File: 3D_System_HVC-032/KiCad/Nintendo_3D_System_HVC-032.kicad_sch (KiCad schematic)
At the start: 45 parts, among them CN1 Famicon Expansion Port, J1 スコープ１, J2 スコープ２, Q1 2SC2120, U1 Sharp IX0043AE, U2 JRC 4558D, X1 4MHz

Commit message: Update Nintendo_3D_System_HVC-032.kicad_sch
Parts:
- C1, C10, C11, C12, C6, C7, C8, C9: footprint (none) -> Capacitor_THT:CP_Radial_D5.0mm_P2.50mm
- C2, C4, C5: footprint (none) -> Capacitor_THT:C_Disc_D3.4mm_W2.1mm_P2.50mm
- CN1: footprint (none) -> Connector_PinHeader_2.54mm:PinHeader_1x03_P2.54mm_Vertical
- D2, D3, D4, D5, D6, ZD1: footprint (none) -> Diode_THT:D_DO-35_SOD27_P7.62mm_Horizontal
- FB1: footprint (none) -> Clueless_Engineer:FB_28L0138-10R-10
- J1, J2: footprint (none) -> Connector_Audio:Jack_3.5mm_CUI_SJ1-3513N_Horizontal
- L1: footprint (none) -> Inductor_THT:L_Axial_L16.0mm_D7.5mm_P25.40mm_Horizontal_Fastron_XHBCC
- Q1: footprint (none) -> Package_TO_SOT_THT:TO-92_Inline
- R1, R10, R11, R12, R13, R14, R15, R16, R17, R18, R19, R2, R3, R4, R5, R6, R7, R8, R9: footprint (none) -> Resistor_THT:R_Axial_DIN0207_L6.3mm_D2.5mm_P7.62mm_Horizontal
- U2: footprint (none) -> Package_DIP:DIP-8_W7.62mm
- X1: footprint (none) -> Crystal:Crystal_HC49-U_Vertical
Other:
- moved on the sheet: C10
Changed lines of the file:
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@@
 		)
 	)
-	(text_box "ZD1 original likely a RD15EB"
+	(text_box "ZD1 original likely an RD15EB"
 		(exclude_from_sim no)
 		(at 143.51 46.99 0)
-		(size 17.78 6.35)
+		(size 19.05 5.08)
 		(margins 0.9525 0.9525 0.9525 0.9525)
 		(stroke
@@
 	(wire
 		(pts
-			(xy 223.52 59.69) (xy 223.52 54.61)
-		)
-		(stroke
-			(width 0)
-			(type default)
-		)
-	)
-	(wire
-		(pts
 			(xy 152.4 63.5) (xy 149.86 63.5)
 		)
@@
 	(wire
 		(pts
-			(xy 223.52 49.53) (xy 223.52 52.07)
+			(xy 223.52 49.53) (xy 223.52 50.8)
 		)
 		(stroke
@@
 	(wire
 		(pts
+			(xy 223.52 58.42) (xy 223.52 59.69)
+		)
+		(stroke
+			(width 0)
+			(type default)
+		)
+	)
+	(wire
+		(pts
 			(xy 80.01 66.04) (xy 87.63 66.04)
 		)
@@
 			)
 		)
-		(property "Footprint" ""
+		(property "Footprint" "Resistor_THT:R_Axial_DIN0207_L6.3mm_D2.5mm_P7.62mm_Horizontal"
 			(at 184.912 74.93 90)
 			(effects
@@
 			)
 		)
-		(property "Footprint" ""
+		(property "Footprint" "Package_DIP:DIP-8_W7.62mm"
 			(at 245.11 46.99 0)
 			(effects
@@
 			)
 		)
-		(property "Footprint" ""
+		(property "Footprint" "Resistor_THT:R_Axial_DIN0207_L6.3mm_D2.5mm_P7.62mm_Horizontal"
 			(at 156.21 65.278 90)
 			(effects
@@
 			)
 		)
-		(property "Footprint" ""
+		(property "Footprint" "Diode_THT:D_DO-35_SOD27_P7.62mm_Horizontal"
 			(at 163.83 43.18 0)
 			(effects
@@
 			)
 		)
-		(property "Footprint" ""
+		(property "Footprint" "Resistor_THT:R_Axial_DIN0207_L6.3mm_D2.5mm_P7.62mm_Horizontal"
 			(at 101.092 175.26 90)
 			(effects
@@
 			)
 		)
-		(property "Footprint" ""
+		(property "Footprint" "Capacitor_THT:CP_Radial_D5.0mm_P2.50mm"
 			(at 21.2852 72.39 0)
 			(effects
@@
 			)
 		)
-		(property "Footprint" ""
+		(property "Footprint" "Resistor_THT:R_Axial_DIN0207_L6.3mm_D2.5mm_P7.62mm_Horizontal"
 			(at 57.15 128.778 90)
 			(effects
@@
 			)
 		)
-		(property "Footprint" ""
+		(property "Footprint" "Resistor_THT:R_Axial_DIN0207_L6.3mm_D2.5mm_P7.62mm_Horizontal"
 			(at 77.47 142.748 90)
 			(effects
@@
 			)
 		)
-		(property "Footprint" ""
+		(property "Footprint" "Clueless_Engineer:FB_28L0138-10R-10"
 			(at 98.552 49.53 90)
 			(effects
@@
 			)
 		)
-		(property "Footprint" ""
+		(property "Footprint" "Inductor_THT:L_Axial_L16.0mm_D7.5mm_P25.40mm_Horizontal_Fastron_XHBCC"
 			(at 186.69 31.75 0)
 			(effects
@@
 			)
 		)
-		(property "Footprint" ""
+		(property "Footprint" "Package_DIP:DIP-8_W7.62mm"
 			(at 76.2 168.91 0)
 			(effects
@@
 			)
 		)
-		(property "Footprint" ""
+		(property "Footprint" "Resistor_THT:R_Axial_DIN0207_L6.3mm_D2.5mm_P7.62mm_Horizontal"
 			(at 57.15 62.738 90)
 			(effects
@@
 			)
 		)
-		(property "Footprint" ""
+		(property "Footprint" "Connector_PinHeader_2.54mm:PinHeader_1x03_P2.54mm_Vertical"
 			(at 33.02 60.96 0)
 			(effects
@@
 			)
 		)
-		(property "Footprint" ""
+		(property "Footprint" "Capacitor_THT:CP_Radial_D5.0mm_P2.50mm"
 			(at 100.33 128.5748 0)
 			(effects
@@
 			)
 		)
-		(property "Footprint" ""
+		(property "Footprint" "Diode_THT:D_DO-35_SOD27_P7.62mm_Horizontal"
 			(at 149.86 74.93 0)
 			(effects
@@
 			)
 		)
-		(property "Footprint" ""
+		(property "Footprint" "Resistor_THT:R_Axial_DIN0207_L6.3mm_D2.5mm_P7.62mm_Horizontal"
 			(at 55.88 169.672 90)
 			(effects
@@
 			)
 		)
-		(property "Footprint" ""
+		(property "Footprint" "Diode_THT:D_DO-35_SOD27_P7.62mm_Horizontal"
 			(at 205.74 41.91 0)
 			(effects
@@
 	(symbol
 		(lib_id "Device:C_Polarized")
-		(at 223.52 55.88 0)
+		(at 223.52 54.61 0)
 		(unit 1)
 		(exclude_from_sim no)
@@
 		(fields_autoplaced yes)
 		(property "Reference" "C10"
-			(at 227.33 53.7209 0)
+			(at 227.33 52.4509 0)
 			(effects
 				(font
@@
 		)
 		(property "Value" "22µF 16V"
-			(at 227.33 56.2609 0)
+			(at 227.33 54.9909 0)
 			(effects
 				(font
@@
 			)
 		)
-		(property "Footprint" ""
-			(at 224.4852 59.69 0)
+		(property "Footprint" "Capacitor_THT:CP_Radial_D5.0mm_P2.50mm"
+			(at 224.4852 58.42 0)
 			(effects
 				(font
@@
 		)
 		(property "Datasheet" "~"
-			(at 223.52 55.88 0)
+			(at 223.52 54.61 0)
 			(effects
 				(font
@@
 		)
 		(property "Description" "Polarized capacitor"
-			(at 223.52 55.88 0)
+			(at 223.52 54.61 0)
 			(effects
 				(font
@@
 			)
 		)
-		(property "Footprint" ""
+		(property "Footprint" "Resistor_THT:R_Axial_DIN0207_L6.3mm_D2.5mm_P7.62mm_Horizontal"
 			(at 60.452 160.02 90)
 			(effects
@@
 			)
 		)
-		(property "Footprint" ""
+		(property "Footprint" "Resistor_THT:R_Axial_DIN0207_L6.3mm_D2.5mm_P7.62mm_Horizontal"
 			(at 132.842 55.88 90)
 			(effects
@@
 			)
 		)
-		(property "Footprint" ""
+		(property "Footprint" "Capacitor_THT:CP_Radial_D5.0mm_P2.50mm"
 			(at 203.2 35.8648 0)
 			(effects
@@
 			)
 		)
-		(property "Footprint" ""
+		(property "Footprint" "Resistor_THT:R_Axial_DIN0207_L6.3mm_D2.5mm_P7.62mm_Horizontal"
 			(at 55.88 168.148 90)
 			(effects
@@
 			)
 		)
-		(property "Footprint" ""
+		(property "Footprint" "Resistor_THT:R_Axial_DIN0207_L6.3mm_D2.5mm_P7.62mm_Horizontal"
 			(at 105.918 134.62 90)
 			(effects
@@
 			)
 		)
-		(property "Footprint" ""
+		(property "Footprint" "Resistor_THT:R_Axial_DIN0207_L6.3mm_D2.5mm_P7.62mm_Horizontal"
 			(at 65.278 119.38 90)
 			(effects
@@
 			)
 		)
-		(property "Footprint" ""
+		(property "Footprint" "Resistor_THT:R_Axial_DIN0207_L6.3mm_D2.5mm_P7.62mm_Horizontal"
 			(at 111.76 170.688 90)
 			(effects
@@
 			)
 		)
-		(property "Footprint" ""
+		(property "Footprint" "Package_TO_SOT_THT:TO-92_Inline"
 			(at 247.65 63.5 0)
 			(effects
@@
 			)
 		)
-		(property "Footprint" ""
+		(property "Footprint" "Resistor_THT:R_Axial_DIN0207_L6.3mm_D2.5mm_P7.62mm_Horizontal"
 			(at 165.608 74.93 90)
 			(effects
@@
 			)
 		)
-		(property "Footprint" ""
+		(property "Footprint" "Resistor_THT:R_Axial_DIN0207_L6.3mm_D2.5mm_P7.62mm_Horizontal"
 			(at 68.072 55.88 90)
 			(effects
@@
 			)
 		)
-		(property "Footprint" ""
+		(property "Footprint" "Capacitor_THT:C_Disc_D3.4mm_W2.1mm_P2.50mm"
 			(at 95.25 44.7548 0)
 			(effects
@@
 			)
 		)
-		(property "Footprint" ""
+		(property "Footprint" "Resistor_THT:R_Axial_DIN0207_L6.3mm_D2.5mm_P7.62mm_Horizontal"
 			(at 76.2 182.118 90)
 			(effects
@@
 			)
 		)
-		(property "Footprint" ""
+		(property "Footprint" "Diode_THT:D_DO-35_SOD27_P7.62mm_Horizontal"
 			(at 158.75 36.83 0)
 			(effects
@@
 			)
 		)
-		(property "Footprint" ""
+		(property "Footprint" "Capacitor_THT:CP_Radial_D5.0mm_P2.50mm"
 			(at 147.32 62.5348 0)
 			(effects
@@
 			)
 		)
-		(property "Footprint" ""
+		(property "Footprint" "Connector_Audio:Jack_3.5mm_CUI_SJ1-3513N_Horizontal"
 			(at 133.35 129.54 0)
 			(effects
@@
 			)
 		)
-		(property "Footprint" ""
+		(property "Footprint" "Connector_Audio:Jack_3.5mm_CUI_SJ1-3513N_Horizontal"
 			(at 132.08 171.45 0)
 			(effects
@@
 			)
 		)
-		(property "Footprint" ""
+		(property "Footprint" "Capacitor_THT:C_Disc_D3.4mm_W2.1mm_P2.50mm"
 			(at 58.42 75.2348 0)
 			(effects
@@
 			)
 		)
-		(property "Footprint" ""
+		(property "Footprint" "Capacitor_THT:CP_Radial_D5.0mm_P2.50mm"
 			(at 99.06 167.9448 0)
 			(effects
@@
 			)
 		)
-		(property "Footprint" ""
+		(property "Footprint" "Crystal:Crystal_HC49-U_Vertical"
 			(at 74.93 80.01 0)
 			(effects
@@
 			)
 		)
-		(property "Footprint" ""
+		(property "Footprint" "Diode_THT:D_DO-35_SOD27_P7.62mm_Horizontal"
 			(at 212.09 36.83 0)
 			(effects
@@
 			)
 		)
-		(property "Footprint" ""
+		(property "Footprint" "Resistor_THT:R_Axial_DIN0207_L6.3mm_D2.5mm_P7.62mm_Horizontal"
 			(at 57.15 133.858 90)
 			(effects
@@
 			)
 		)
-		(property "Footprint" ""
+		(property "Footprint" "Capacitor_THT:CP_Radial_D5.0mm_P2.50mm"
 			(at 168.91 37.7952 0)
 			(effects
@@
 			)
 		)
-		(property "Footprint" ""
+		(property "Footprint" "Resistor_THT:R_Axial_DIN0207_L6.3mm_D2.5mm_P7.62mm_Horizontal"
 			(at 114.3 131.318 90)
 			(effects
@@
 			)
 		)
-		(property "Footprint" ""
+		(property "Footprint" "Resistor_THT:R_Axial_DIN0207_L6.3mm_D2.5mm_P7.62mm_Horizontal"
 			(at 119.38 62.738 90)
 			(effects
@@
 			)
 		)
-		(property "Footprint" ""
+		(property "Footprint" "Package_DIP:DIP-8_W7.62mm"
 			(at 77.47 129.54 0)
 			(effects
@@
 			)
 		)
-		(property "Footprint" ""
+		(property "Footprint" "Diode_THT:D_DO-35_SOD27_P7.62mm_Horizontal"
 			(at 163.83 55.88 0)
 			(effects
@@
 			)
 		)
-		(property "Footprint" ""
+		(property "Footprint" "Capacitor_THT:CP_Radial_D5.0mm_P2.50mm"
 			(at 224.4852 46.99 0)
 			(effects
@@
 			)
 		)
-		(property "Footprint" ""
+		(property "Footprint" "Capacitor_THT:C_Disc_D3.4mm_W2.1mm_P2.50mm"
 			(at 58.42 82.8548 0)
 			(effects

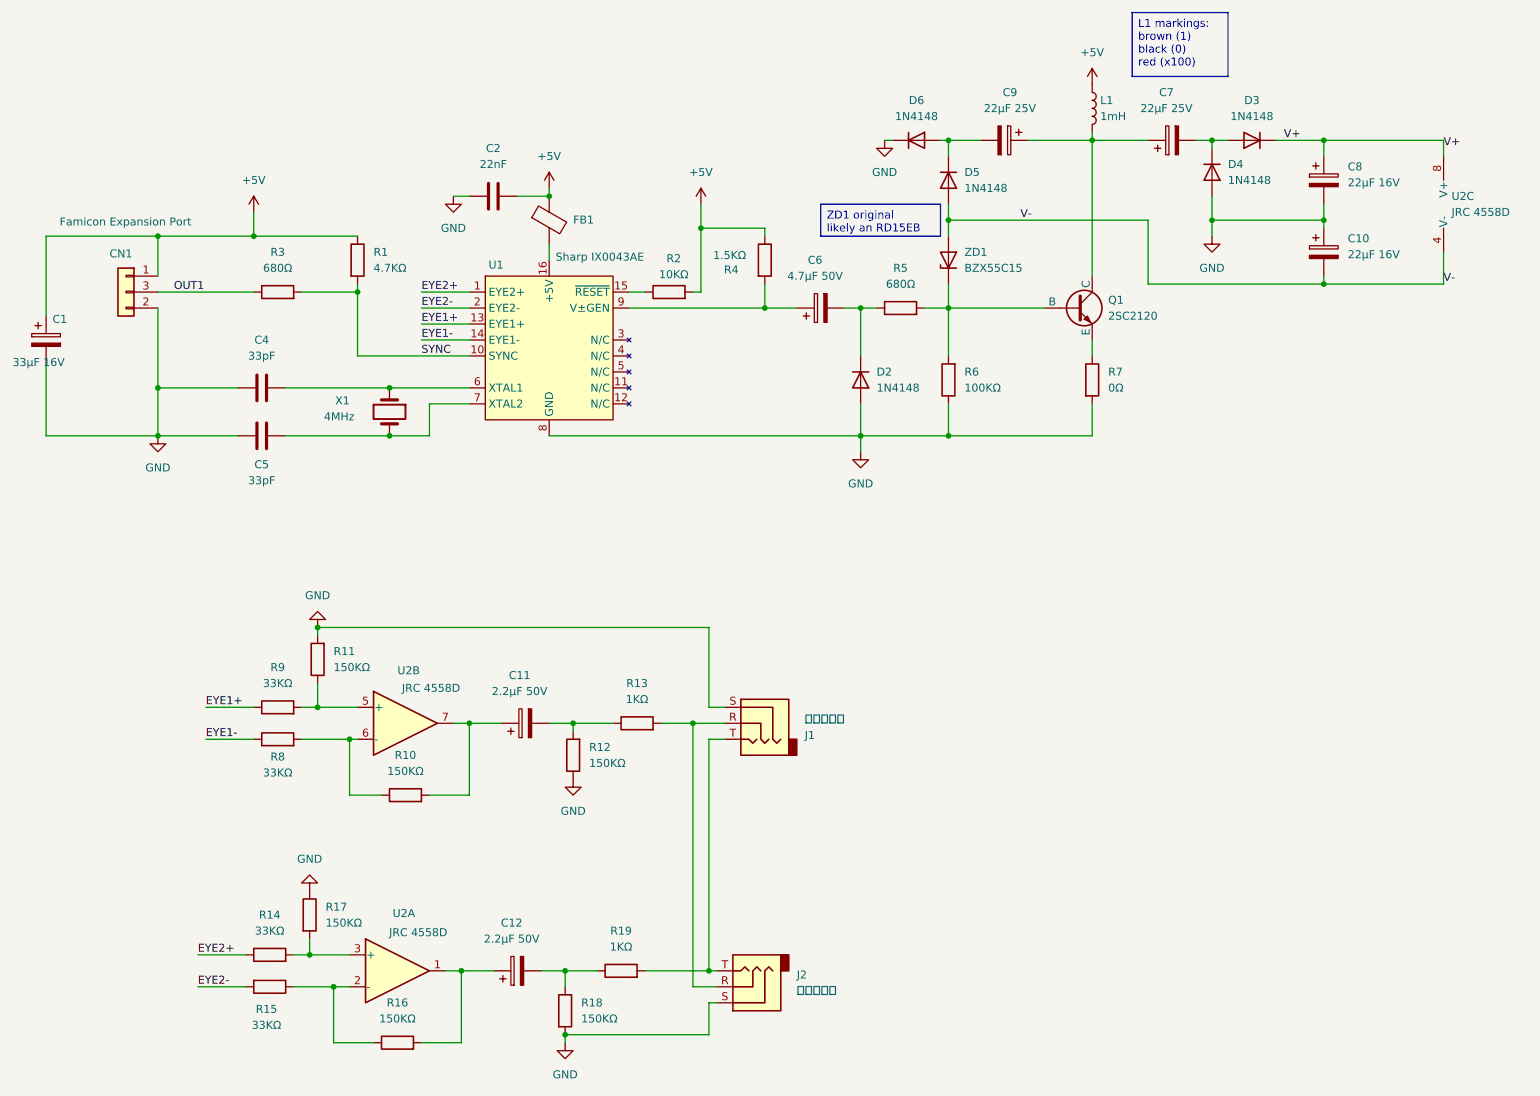
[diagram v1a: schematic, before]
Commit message: Renamed L/R signals
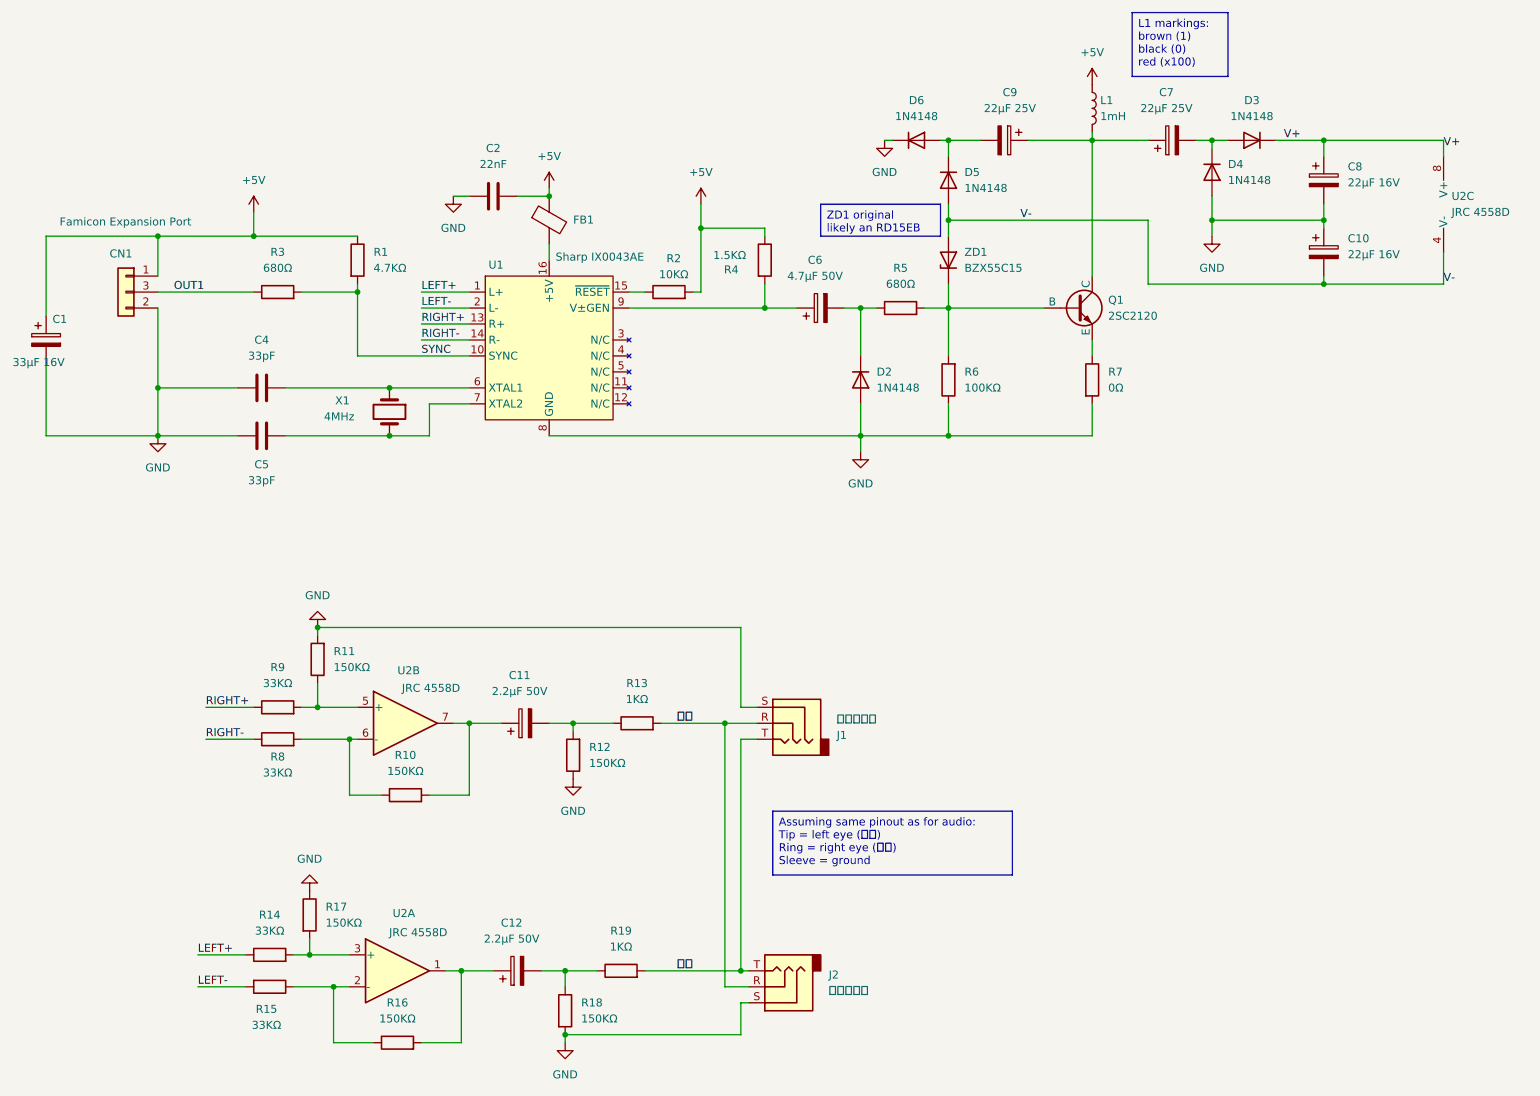
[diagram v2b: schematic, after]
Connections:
- net 左目: now reaches J1.T, J2.T, R19.2
- net 右目: now reaches J1.R, J2.R, R13.2
- net EYE1+ renamed RIGHT+
- net EYE1- renamed RIGHT-
- net EYE2+ renamed LEFT+
- net EYE2- renamed LEFT-
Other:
- moved on the sheet: J1, J2
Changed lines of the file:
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@@
 		(comment 4 "Based on original drawn by Krzysiobal (NESDEV)")
 	)
+	(text_box "Assuming same pinout as for audio:\nTip = left eye (左目)\nRing = right eye (右目)\nSleeve = ground"
+		(exclude_from_sim no)
+		(at 135.89 143.51 0)
+		(size 38.1 10.16)
+		(margins 0.9525 0.9525 0.9525 0.9525)
+		(stroke
+			(width 0)
+			(type solid)
+		)
+		(fill
+			(type none)
+		)
+		(effects
+			(font
+				(size 1.27 1.27)
+			)
+			(justify left top)
+		)
+	)
 	(text_box "L1 markings:\nbrown (1)\nblack (0)\nred (x100)"
 		(exclude_from_sim no)
@@
 	)
 	(junction
-		(at 125.73 168.91)
+		(at 130.81 168.91)
 		(diameter 0)
 		(color 0 0 0 0)
@@
 	)
 	(junction
-		(at 123.19 129.54)
+		(at 128.27 129.54)
 		(diameter 0)
 		(color 0 0 0 0)
@@
 	(wire
 		(pts
-			(xy 125.73 168.91) (xy 115.57 168.91)
-		)
-		(stroke
-			(width 0)
-			(type default)
-		)
-	)
-	(wire
-		(pts
 			(xy 104.14 129.54) (xy 100.33 129.54)
 		)
@@
 	(wire
 		(pts
-			(xy 123.19 129.54) (xy 118.11 129.54)
-		)
-		(stroke
-			(width 0)
-			(type default)
-		)
-	)
-	(wire
-		(pts
 			(xy 102.87 180.34) (xy 102.87 179.07)
 		)
@@
 	(wire
 		(pts
+			(xy 118.11 129.54) (xy 128.27 129.54)
+		)
+		(stroke
+			(width 0)
+			(type default)
+		)
+	)
+	(wire
+		(pts
 			(xy 69.85 71.12) (xy 87.63 71.12)
 		)
@@
 	(wire
 		(pts
-			(xy 128.27 127) (xy 125.73 127)
+			(xy 133.35 127) (xy 130.81 127)
 		)
 		(stroke
@@
 	(wire
 		(pts
-			(xy 127 168.91) (xy 125.73 168.91)
+			(xy 132.08 168.91) (xy 130.81 168.91)
 		)
 		(stroke
@@
 	(wire
 		(pts
-			(xy 128.27 129.54) (xy 123.19 129.54)
+			(xy 133.35 129.54) (xy 128.27 129.54)
 		)
 		(stroke
@@
 	(wire
 		(pts
-			(xy 123.19 171.45) (xy 123.19 129.54)
+			(xy 128.27 171.45) (xy 128.27 129.54)
 		)
 		(stroke
@@
 	(wire
 		(pts
-			(xy 125.73 132.08) (xy 125.73 168.91)
+			(xy 130.81 132.08) (xy 130.81 168.91)
 		)
 		(stroke
@@
 	(wire
 		(pts
-			(xy 125.73 127) (xy 125.73 114.3)
+			(xy 130.81 127) (xy 130.81 114.3)
 		)
 		(stroke
@@
 	(wire
 		(pts
-			(xy 128.27 132.08) (xy 125.73 132.08)
+			(xy 133.35 132.08) (xy 130.81 132.08)
 		)
 		(stroke
@@
 	(wire
 		(pts
+			(xy 115.57 168.91) (xy 130.81 168.91)
+		)
+		(stroke
+			(width 0)
+			(type default)
+		)
+	)
+	(wire
+		(pts
 			(xy 87.63 78.74) (xy 81.28 78.74)
 		)
@@
 	(wire
 		(pts
-			(xy 125.73 173.99) (xy 125.73 179.07)
+			(xy 130.81 173.99) (xy 130.81 179.07)
 		)
 		(stroke
@@
 	(wire
 		(pts
-			(xy 125.73 179.07) (xy 102.87 179.07)
+			(xy 130.81 179.07) (xy 102.87 179.07)
 		)
 		(stroke
@@
 	(wire
 		(pts
-			(xy 127 171.45) (xy 123.19 171.45)
+			(xy 132.08 171.45) (xy 128.27 171.45)
 		)
 		(stroke
@@
 	(wire
 		(pts
-			(xy 127 173.99) (xy 125.73 173.99)
+			(xy 132.08 173.99) (xy 130.81 173.99)
 		)
 		(stroke
@@
 	(wire
 		(pts
-			(xy 125.73 114.3) (xy 63.5 114.3)
+			(xy 130.81 114.3) (xy 63.5 114.3)
 		)
 		(stroke
@@
 		)
 	)
-	(label "EYE2-"
+	(label "LEFT-"
 		(at 80.01 63.5 0)
 		(effects
@@
 		)
 	)
-	(label "EYE2+"
+	(label "LEFT+"
 		(at 80.01 60.96 0)
 		(effects
@@
 		)
 	)
-	(label "EYE2+"
+	(label "LEFT+"
 		(at 44.45 166.37 0)
 		(effects
@@
 		)
 	)
-	(label "EYE2-"
+	(label "LEFT-"
 		(at 44.45 171.45 0)
 		(effects
@@
 		)
 	)
-	(label "EYE1-"
+	(label "RIGHT-"
 		(at 80.01 68.58 0)
 		(effects
@@
 		)
 	)
-	(label "EYE1+"
+	(label "RIGHT+"
 		(at 45.72 127 0)
 		(effects
@@
 		)
 	)
-	(label "EYE1-"
+	(label "RIGHT-"
 		(at 45.72 132.08 0)
 		(effects
@@
 		)
 	)
-	(label "EYE1+"
+	(label "左目"
+		(at 120.65 168.91 0)
+		(effects
+			(font
+				(size 1.27 1.27)
+			)
+			(justify left bottom)
+		)
+	)
+	(label "RIGHT+"
 		(at 80.01 66.04 0)
 		(effects
@@
 		)
 	)
+	(label "右目"
+		(at 120.65 129.54 0)
+		(effects
+			(font
+				(size 1.27 1.27)
+			)
+			(justify left bottom)
+		)
+	)
 	(symbol
 		(lib_id "Device:R")
@@
 	(symbol
 		(lib_id "Connector_Audio:AudioJack3")
-		(at 133.35 129.54 0)
+		(at 138.43 129.54 0)
 		(mirror y)
 		(unit 1)
@@
 		(dnp no)
 		(property "Reference" "J1"
-			(at 140.97 131.4451 0)
+			(at 146.05 131.4451 0)
 			(effects
 				(font
@@
 		)
 		(property "Value" "スコープ１"
-			(at 140.97 128.9051 0)
+			(at 146.05 128.9051 0)
 			(effects
 				(font
@@
 		)
 		(property "Footprint" "Connector_Audio:Jack_3.5mm_CUI_SJ1-3513N_Horizontal"
-			(at 133.35 129.54 0)
+			(at 138.43 129.54 0)
 			(effects
 				(font
@@
 		)
 		(property "Datasheet" "~"
-			(at 133.35 129.54 0)
+			(at 138.43 129.54 0)
 			(effects
 				(font
@@
 		)
 		(property "Description" "Audio Jack, 3 Poles (Stereo / TRS)"
-			(at 133.35 129.54 0)
+			(at 138.43 129.54 0)
 			(effects
 				(font
@@
 	(symbol
 		(lib_id "Connector_Audio:AudioJack3")
-		(at 132.08 171.45 180)
+		(at 137.16 171.45 180)
 		(unit 1)
 		(exclude_from_sim no)
@@
 		(fields_autoplaced yes)
 		(property "Reference" "J2"
-			(at 139.7 169.5449 0)
+			(at 144.78 169.5449 0)
 			(effects
 				(font
@@
 		)
 		(property "Value" "スコープ２"
-			(at 139.7 172.0849 0)
+			(at 144.78 172.0849 0)
 			(effects
 				(font
@@
 		)
 		(property "Footprint" "Connector_Audio:Jack_3.5mm_CUI_SJ1-3513N_Horizontal"
-			(at 132.08 171.45 0)
+			(at 137.16 171.45 0)
 			(effects
 				(font
@@
 		)
 		(property "Datasheet" "~"
-			(at 132.08 171.45 0)
+			(at 137.16 171.45 0)
 			(effects
 				(font
@@
 		)
 		(property "Description" "Audio Jack, 3 Poles (Stereo / TRS)"
-			(at 132.08 171.45 0)
+			(at 137.16 171.45 0)
 			(effects
 				(font
